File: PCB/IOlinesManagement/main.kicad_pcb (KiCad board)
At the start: 4 copper layers, 150.7 x 92.4 mm, 259 parts, among them K1 HK19F-DCxxV-SHC, K10 HK19F-DCxxV-SHC, K11 HK19F-DCxxV-SHC, K12 HK19F-DCxxV-SHC, K13 HK19F-DCxxV-SHC, K14 HK19F-DCxxV-SHC, K15 HK19F-DCxxV-SHC, K16 HK19F-DCxxV-SHC, K2 HK19F-DCxxV-SHC, K3 HK19F-DCxxV-SHC, K4 HK19F-DCxxV-SHC, K5 HK19F-DCxxV-SHC, K6 HK19F-DCxxV-SHC, K7 HK19F-DCxxV-SHC, K8 HK19F-DCxxV-SHC, K9 HK19F-DCxxV-SHC, Q1 BC817, Q10 BC817, Q11 BC817, Q12 BC817, Q13 BC817, Q14 BC817, Q15 BC817, Q16 BC817, Q17 BC327, Q18 BC337, Q19 BC327, Q2 BC817, Q20 BC337, Q21 BC327, Q22 BC337, Q23 BC327, Q24 BC337, Q25 BC327, Q26 BC327, Q27 BC337, Q28 BC327, Q29 BC337, Q3 BC817, Q30 BC327, Q31 BC337, Q32 BC327, Q33 BC337, Q34 BC327, Q35 BC327, Q36 BC337, Q37 BC327, Q38 BC337, Q39 BC327, Q4 BC817, Q40 BC337, Q41 BC327, Q42 BC337, Q43 BC327, Q44 BC337, Q45 BC327, Q46 BC337, Q47 BC327, Q48 BC337, Q49 BC327, Q5 BC817, Q50 BC337, Q51 BC327, Q52 BC327, Q53 BC327, Q54 BC327, Q55 BC327, Q56 BC327, Q57 BC327, Q58 BC327, Q59 BC327, Q6 BC817, Q60 BC327, Q61 BC327, Q62 BC327, Q63 BC327, Q64 BC327, Q7 BC817, Q8 BC817, Q9 BC817

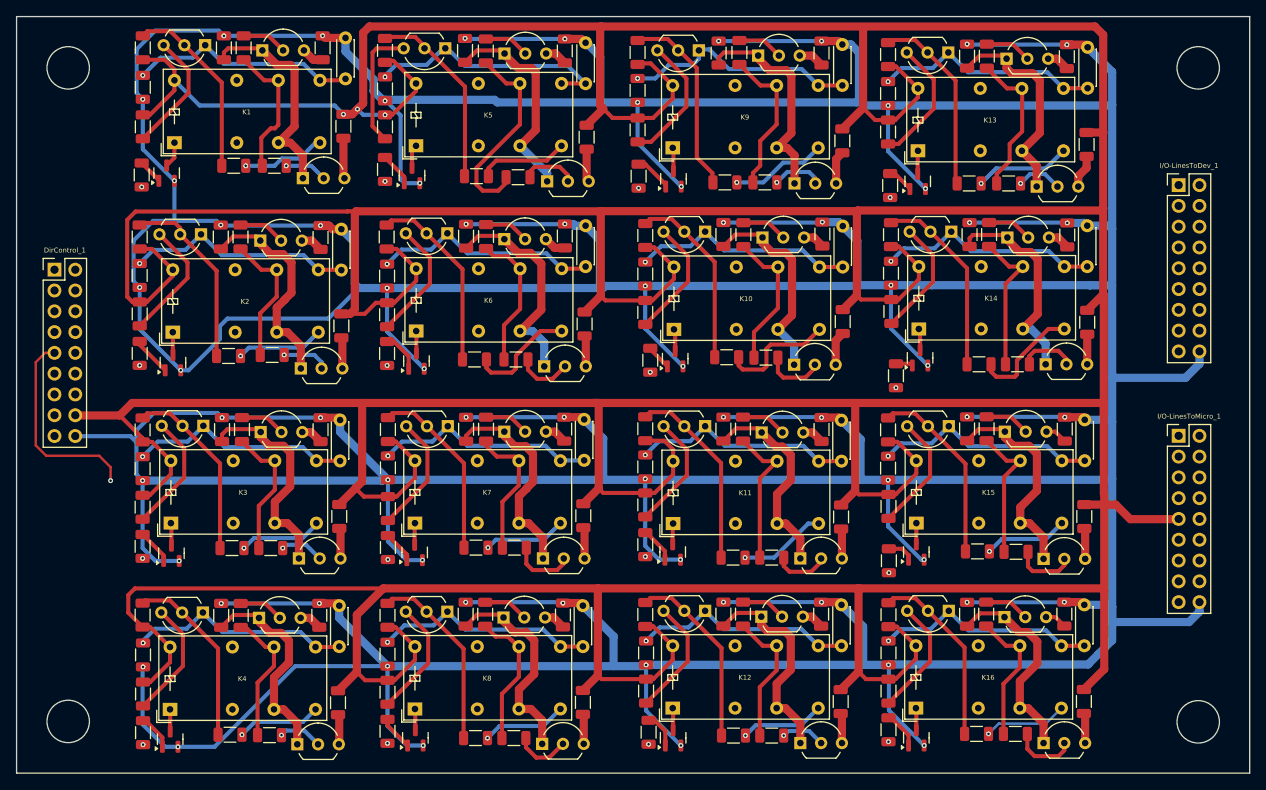
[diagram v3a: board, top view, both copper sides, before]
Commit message: New version based on MIC4427 push-pull driver
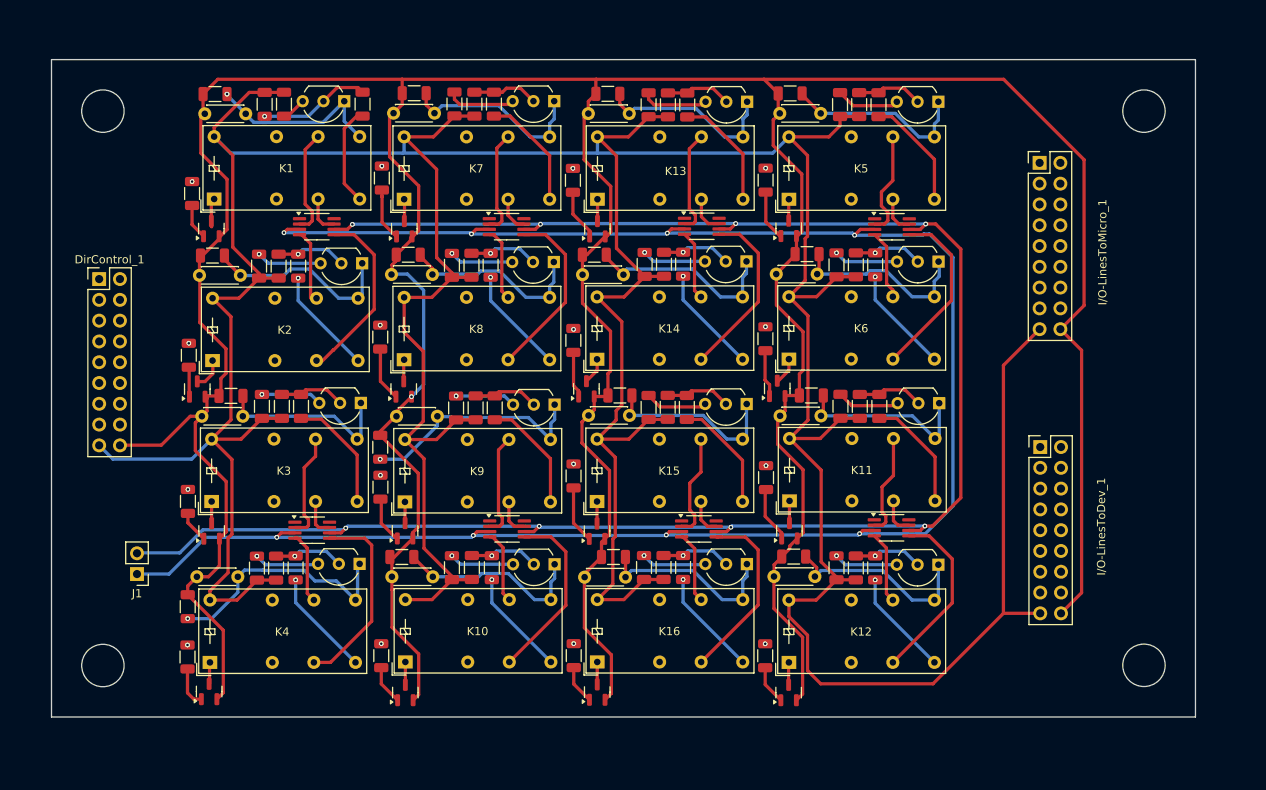
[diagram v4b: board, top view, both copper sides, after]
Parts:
- removed Q17, Q19, Q21, Q23, Q26, Q28, Q30, Q32, Q35, Q37, Q39, Q41, Q43, Q45, Q47, Q49: BC327, Package_TO_SOT_THT:TO-92_Inline_Wide
- removed Q18, Q20, Q22, Q24, Q27, Q29, Q31, Q33, Q36, Q38, Q40, Q42, Q44, Q46, Q48, Q50: BC337, Package_TO_SOT_THT:TO-92_Inline_Wide
- removed R100, R101, R104, R21, R24, R25, R28, R29, R32, R33, R36, R42, R45, R46, R49, R50, R53, R57, R60, R66, R69, R70, R73, R74, R77, R78, R81, R89, R92, R93, R96, R97: 50, Resistor_SMD:R_1206_3216Metric
- removed R102, R103, R22, R23, R26, R27, R30, R31, R34, R35, R43, R44, R47, R48, R51, R52, R58, R59, R67, R68, R71, R72, R75, R76, R79, R80, R90, R91, R94, R95, R98, R99: 5K, Resistor_SMD:R_1206_3216Metric
- removed R143: 1K, Resistor_SMD:R_1206_3216Metric
- removed R18, R19, R20, R37, R38, R39, R41, R61, R62, R63, R64, R85, R86, R87, R88: 100K, Resistor_SMD:R_1206_3216Metric
- added J1: Conn_01x02, Connector_PinHeader_2.54mm:PinHeader_1x02_P2.54mm_Vertical, F.Cu at (77.9, 122.1)
- added U1: MIC4427, Package_SO:MSOP-8_3x3mm_P0.65mm, F.Cu at (99.9, 79.7)
- added U2: MIC4427, Package_SO:MSOP-8_3x3mm_P0.65mm, F.Cu at (99.3, 116.8)
- added U3: MIC4427, Package_SO:MSOP-8_3x3mm_P0.65mm, F.Cu at (170.2, 79.7)
- added U4: MIC4427, Package_SO:MSOP-8_3x3mm_P0.65mm, F.Cu at (123.1, 79.7)
- added U5: MIC4427, Package_SO:MSOP-8_3x3mm_P0.65mm, F.Cu at (123.1, 116.6)
- added U6: MIC4427, Package_SO:MSOP-8_3x3mm_P0.65mm, F.Cu at (170.1, 116.5)
- added U7: MIC4427, Package_SO:MSOP-8_3x3mm_P0.65mm, F.Cu at (146.9, 79.7)
- added U8: MIC4427, Package_SO:MSOP-8_3x3mm_P0.65mm, F.Cu at (146.6, 116.6)
- R17: value 100K -> 1K
- moved C6 63.9 mm to (114.6, 102.9), turned to 180 degrees
- moved C4 62.8 mm to (114.0, 122.5), turned to 180 degrees
- moved Q53 60.6 mm to (175.8, 64.4)
- moved Q59 60.1 mm to (175.8, 84.0)
- moved R121 58.3 mm to (166.1, 64.8)
- moved R116 57.8 mm to (121.1, 84.4), turned to 90 degrees
- moved R144 57.4 mm to (165.7, 84.4)
- moved C15 56.7 mm to (137.6, 122.5), turned to 180 degrees
- moved C12 56.7 mm to (137.3, 85.6), turned to 180 degrees
- moved C14 56.1 mm to (138.0, 65.9), turned to 180 degrees
- moved C16 55.9 mm to (138.1, 102.8), turned to 180 degrees
- moved R114 55.7 mm to (163.8, 64.8), turned to -90 degrees
- moved K9 54.2 mm to (110.6, 113.3)
- moved R153 54.2 mm to (121.5, 64.7), turned to 90 degrees
- moved Q10 54.1 mm to (110.7, 116.9)
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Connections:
- DirControl_1 pad 1: DIR-13 -> DIR-1
- DirControl_1 pad 10: DIR-3 -> DIR-11
- DirControl_1 pad 11: DIR-16 -> DIR-10
- DirControl_1 pad 12: DIR-7 -> DIR-15
- DirControl_1 pad 13: DIR-12 -> DIR-16
- DirControl_1 pad 14: DIR-11 -> DIR-9
- DirControl_1 pad 15: DIR-8 -> DIR-12
- DirControl_1 pad 16: +5V -> DIR-3
- DirControl_1 pad 17: DIR-4 -> +5V
- DirControl_1 pad 2: DIR-2 -> DIR-6
- DirControl_1 pad 3: DIR-9 -> DIR-7
- DirControl_1 pad 4: DIR-6 -> DIR-14
- DirControl_1 pad 5: DIR-5 -> DIR-13
- DirControl_1 pad 6: DIR-10 -> DIR-8
- DirControl_1 pad 7: DIR-1 -> DIR-5
- DirControl_1 pad 8: DIR-14 -> DIR-2
- DirControl_1 pad 9: DIR-15 -> DIR-4
- I/O-LinesToDev_1 pad 10: unconnected-(I/O-LinesToDev_1-Pin_10-Pad10) -> I/O-4 Port
- I/O-LinesToDev_1 pad 11: I/O-15 Port -> I/O-9 Port
- I/O-LinesToDev_1 pad 12: I/O-16 Port -> I/O-10 Port
- I/O-LinesToDev_1 pad 13: I/O-11 Port -> I/O-15 Port
- I/O-LinesToDev_1 pad 14: I/O-12 Port -> I/O-16 Port
- I/O-LinesToDev_1 pad 15: I/O-7 Port -> I/O-11 Port
- I/O-LinesToDev_1 pad 16: I/O-8 Port -> I/O-12 Port
- I/O-LinesToDev_1 pad 17: I/O-4 Port -> +5V
- I/O-LinesToDev_1 pad 2: I/O-13 Port -> I/O-5 Port
- I/O-LinesToDev_1 pad 3: I/O-6 Port -> I/O-8 Port
- I/O-LinesToDev_1 pad 4: I/O-5 Port -> I/O-13 Port
- I/O-LinesToDev_1 pad 5: I/O-10 Port -> I/O-14 Port
- I/O-LinesToDev_1 pad 6: I/O-9 Port -> I/O-7 Port
- I/O-LinesToDev_1 pad 7: I/O-14 Port -> I/O-6 Port
- I/O-LinesToMicro_1 pad 1: I/O-14 Micro -> I/O-6 Micro
- I/O-LinesToMicro_1 pad 12: I/O-8 Micro -> I/O-10 Micro
- I/O-LinesToMicro_1 pad 13: I/O-11 Micro -> I/O-9 Micro
- I/O-LinesToMicro_1 pad 14: I/O-12 Micro -> I/O-16 Micro
- I/O-LinesToMicro_1 pad 15: I/O-7 Micro -> I/O-3 Micro
- I/O-LinesToMicro_1 pad 16: I/O-16 Micro -> I/O-12 Micro
- I/O-LinesToMicro_1 pad 17: I/O-3 Micro -> +5V
- I/O-LinesToMicro_1 pad 3: I/O-10 Micro -> I/O-14 Micro
- I/O-LinesToMicro_1 pad 4: I/O-5 Micro -> I/O-7 Micro
- I/O-LinesToMicro_1 pad 5: I/O-6 Micro -> I/O-8 Micro
- I/O-LinesToMicro_1 pad 6: I/O-9 Micro -> I/O-13 Micro
- I/O-LinesToMicro_1 pad 8: I/O-13 Micro -> I/O-5 Micro
- I/O-LinesToMicro_1 pad 9: +5V -> I/O-11 Micro
- R17 pad 1: GND -> Net-(Q59-E)
- R17 pad 2: OutputToDev_9 -> +5V
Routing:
- net GND: track 1159.9 -> 536.7 mm, vias 64 -> 1
- net +5V: track 988.5 -> 562.8 mm, vias 3 -> 0
- net Net-(J1-Pin_1): track 0.00 -> 234.9 mm, vias 0 -> 8
- net Net-(J1-Pin_2): track 0.00 -> 227.5 mm, vias 0 -> 8
- net I/O-5 Micro: track 135.9 -> 41.6 mm
- net I/O-6 Micro: track 105.6 -> 33.3 mm
- net I/O-12 Port: track 104.9 -> 33.2 mm
- net DIR-15: track 131.1 -> 63.3 mm, vias 2 -> 1
- net DIR-16: track 147.9 -> 83.0 mm
- net I/O-1 Micro: track 161.7 -> 98.5 mm
- net I/O-6 Port: track 91.9 -> 36.2 mm
- net I/O-5 Port: track 102.9 -> 49.0 mm
- net I/O-11 Port: track 80.3 -> 27.7 mm
- net I/O-16 Micro: track 36.8 -> 86.8 mm
- net DIR-14: track 105.9 -> 56.8 mm
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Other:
- board size 150.7 x 92.4 mm -> 139.8 x 80.3 mm

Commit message: Small fix
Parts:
- moved R1 0.40 mm to (84.2, 95.0)
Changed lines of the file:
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@@
 	(footprint "Resistor_SMD:R_1206_3216Metric"
 		(layer "F.Cu")
-		(at 84.234123 95.416987 90)
+		(at 84.2264 95.0214 90)
 		(descr "Resistor SMD 1206 (3216 Metric), square (rectangular) end terminal, IPC-7351 nominal, (Body size source: IPC-SM-782 page 72, https://www.pcb-3d.com/wordpress/wp-content/uploads/ipc-sm-782a_amendment_1_and_2.pdf), generated with kicad-footprint-generator")
 		(tags "resistor")
@@
 			(keep_text_aligned yes)
 		)
-		(gr_text "139,777"
+		(gr_text "139.777"
 			(at 141.379003 148.717 0)
 			(layer "Eco1.User")
@@
 	(segment
 		(start 84.2772 96.922564)
-		(end 84.234123 96.879487)
+		(end 84.2264 96.871764)
 		(width 0.4)
 		(layer "F.Cu")
@@
 		(net 111)
 	)
+	(segment
+		(start 84.2264 96.871764)
+		(end 84.2264 96.4839)
+		(width 0.4)
+		(layer "F.Cu")
+		(net 111)
+	)
 	(via
-		(at 84.234123 93.954487)
+		(at 84.2264 93.5589)
 		(size 0.6)
 		(drill 0.3)
@@
 	)
 	(segment
-		(start 84.234123 93.954487)
-		(end 76.047487 93.954487)
+		(start 84.2264 93.5589)
+		(end 83.830813 93.954487)
 		(width 0.4)
 		(layer "In1.Cu")
@@
 		(width 0.4)
 		(layer "In1.Cu")
+		(net 112)
+	)
+	(segment
+		(start 83.830813 93.954487)
+		(end 76.047487 93.954487)
+		(width 0.4)
+		(layer "In1.Cu")

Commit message: Small size reduction
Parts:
- moved J1 1.65 mm to (76.3, 121.7)
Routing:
- net Net-(J1-Pin_1): track 234.9 -> 236.7 mm
- net Net-(J1-Pin_2): track 227.5 -> 229.2 mm
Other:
- board size 139.8 x 80.3 mm -> 138.4 x 80.3 mm
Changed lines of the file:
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@@
 	(footprint "Connector_PinHeader_2.54mm:PinHeader_1x02_P2.54mm_Vertical"
 		(layer "F.Cu")
-		(at 77.9018 122.1486 180)
+		(at 76.327 121.666 180)
 		(descr "Through hole straight pin header, 1x02, 2.54mm pitch, single row")
 		(tags "Through hole pin header THT 1x02 2.54mm single row")
@@
 	)
 	(gr_rect
-		(start 73.6092 114.935)
-		(end 82.1436 127.2794)
+		(start 71.9836 114.2746)
+		(end 80.518 126.619)
 		(stroke
 			(width 0.1)
@@
 	)
 	(gr_rect
-		(start 67.454 59.2904)
+		(start 68.851 59.2904)
 		(end 207.231 139.6168)
 		(stroke
@@
 	)
 	(gr_circle
-		(center 73.7362 133.3246)
-		(end 76.327 133.3246)
+		(center 75.184 133.2992)
+		(end 77.7748 133.2992)
 		(stroke
 			(width 0.05)
@@
 	)
 	(gr_circle
-		(center 73.7362 65.5828)
-		(end 76.327 65.5828)
+		(center 75.184 65.5828)
+		(end 77.7748 65.5828)
 		(stroke
 			(width 0.05)
@@
 	)
 	(gr_circle
-		(center 73.7362 133.3246)
-		(end 79.7306 133.3246)
+		(center 75.184 133.2992)
+		(end 81.1784 133.2992)
 		(stroke
 			(width 0.1)
@@
 	)
 	(gr_circle
-		(center 73.7362 65.5828)
-		(end 79.7306 65.5828)
+		(center 75.184 65.5828)
+		(end 81.1784 65.5828)
 		(stroke
 			(width 0.1)
@@
 		(layer "Eco1.User")
 		(pts
-			(xy 67.454 139.6168) (xy 207.231 139.6168)
+			(xy 68.851 139.6168) (xy 207.231 139.6168)
 		)
 		(height 5.2902)
@@
 			(keep_text_aligned yes)
 		)
-		(gr_text "139.777"
-			(at 141.379003 148.717 0)
+		(gr_text "138,38"
+			(at 142.037157 148.717 0)
 			(layer "Eco1.User")
 			(effects
@@
 	)
 	(segment
+		(start 77.9526 119.5578)
+		(end 77.5208 119.126)
+		(width 0.4)
+		(layer "B.Cu")
+		(net 180)
+	)
+	(segment
 		(start 174.2694 79.375)
 		(end 151.1046 79.375)
@@
 	)
 	(segment
-		(start 150.622 116.2812)
-		(end 150.4696 116.4336)
+		(start 85.9536 116.7384)
+		(end 83.1342 119.5578)
 		(width 0.4)
 		(layer "B.Cu")
@@
 	)
 	(segment
-		(start 174.1678 116.2812)
-		(end 150.622 116.2812)
+		(start 103.2002 116.7384)
+		(end 85.9536 116.7384)
 		(width 0.4)
 		(layer "B.Cu")
@@
 	)
 	(segment
-		(start 103.4034 116.5352)
-		(end 103.2002 116.7384)
+		(start 150.622 116.2812)
+		(end 150.4696 116.4336)
 		(width 0.4)
 		(layer "B.Cu")
@@
 	)
 	(segment
-		(start 104.2416 79.4004)
-		(end 104.2162 79.4258)
+		(start 77.5208 119.126)
+		(end 76.327 119.126)
 		(width 0.4)
 		(layer "B.Cu")
@@
 	)
 	(segment
-		(start 103.2002 116.7384)
-		(end 85.9536 116.7384)
+		(start 174.1678 116.2812)
+		(end 150.622 116.2812)
 		(width 0.4)
 		(layer "B.Cu")
@@
 	)
 	(segment
-		(start 150.4696 116.4336)
-		(end 127.1778 116.4336)
+		(start 104.2416 79.4004)
+		(end 104.2162 79.4258)
 		(width 0.4)
 		(layer "B.Cu")
@@
 	)
 	(segment
-		(start 127.1778 116.4336)
-		(end 127.0508 116.3066)
+		(start 103.4034 116.5352)
+		(end 103.2002 116.7384)
 		(width 0.4)
 		(layer "B.Cu")
@@
 	)
 	(segment
-		(start 151.0538 79.3242)
-		(end 127.2794 79.3242)
+		(start 83.1342 119.5578)
+		(end 77.9526 119.5578)
 		(width 0.4)
 		(layer "B.Cu")
@@
 	)
 	(segment
-		(start 77.9526 119.5578)
-		(end 77.9018 119.6086)
+		(start 150.4696 116.4336)
+		(end 127.1778 116.4336)
 		(width 0.4)
 		(layer "B.Cu")
@@
 	)
 	(segment
-		(start 85.9536 116.7384)
-		(end 83.1342 119.5578)
+		(start 127.1778 116.4336)
+		(end 127.0508 116.3066)
 		(width 0.4)
 		(layer "B.Cu")
@@
 	)
 	(segment
-		(start 127.0508 116.3066)
-		(end 103.632 116.3066)
+		(start 151.0538 79.3242)
+		(end 127.2794 79.3242)
 		(width 0.4)
 		(layer "B.Cu")
@@
 	)
 	(segment
-		(start 127.2032 79.4004)
-		(end 104.2416 79.4004)
+		(start 127.0508 116.3066)
+		(end 103.632 116.3066)
 		(width 0.4)
 		(layer "B.Cu")
@@
 	)
 	(segment
-		(start 83.1342 119.5578)
-		(end 77.9526 119.5578)
+		(start 127.2032 79.4004)
+		(end 104.2416 79.4004)
 		(width 0.4)
 		(layer "B.Cu")
@@
 	)
 	(segment
-		(start 81.8134 122.1486)
-		(end 77.9018 122.1486)
-		(width 0.4)
-		(layer "B.Cu")
-		(net 182)
-	)
-	(segment
 		(start 118.9863 117.4369)
 		(end 142.5067 117.4369)
@@
 	)
 	(segment
+		(start 94.9833 117.6655)
+		(end 86.2965 117.6655)
+		(width 0.4)
+		(layer "B.Cu")
+		(net 182)
+	)
+	(segment
 		(start 177.5968 113.843564)
 		(end 177.5968 83.4644)
@@
 	)
 	(segment
-		(start 94.9833 117.6655)
-		(end 86.2965 117.6655)
+		(start 76.8096 122.1486)
+		(end 76.327 121.666)
+		(width 0.4)
+		(layer "B.Cu")
+		(net 182)
+	)
+	(segment
+		(start 86.2965 117.6655)
+		(end 81.8134 122.1486)
 		(width 0.4)
 		(layer "B.Cu")
@@
 	)
 	(segment
+		(start 81.8134 122.1486)
+		(end 76.8096 122.1486)
+		(width 0.4)
+		(layer "B.Cu")
+		(net 182)
+	)
+	(segment
 		(start 174.219364 117.221)
 		(end 177.5968 113.843564)
@@
 		(width 0.4)
 		(layer "B.Cu")
-		(net 182)
-	)
-	(segment
-		(start 86.2965 117.6655)
-		(end 81.8134 122.1486)
-		(width 0.4)
-		(layer "B.Cu")
